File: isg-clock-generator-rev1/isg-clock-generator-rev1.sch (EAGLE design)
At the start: 162 parts, among them IC1 LMK03318RHSR, IC4 TPS7A8001DRBR, IC5 TPS7A8001DRBR, Q1 7M50072001, X1 OUT2_P, X2 OUT2_N, X3 OUT0_P, X4 PRIREF_P, X5 PRIREF_N, X6 V_IN_EXT

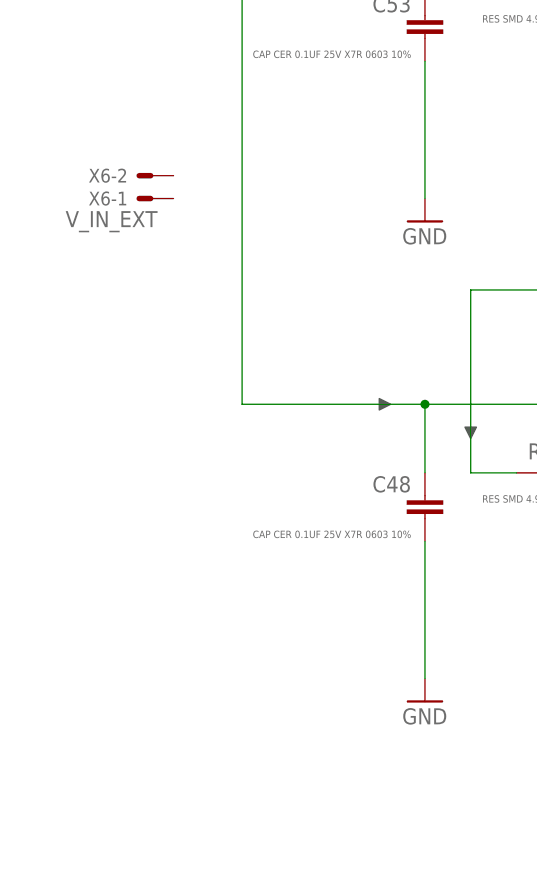
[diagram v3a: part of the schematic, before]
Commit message: First-pass routing done
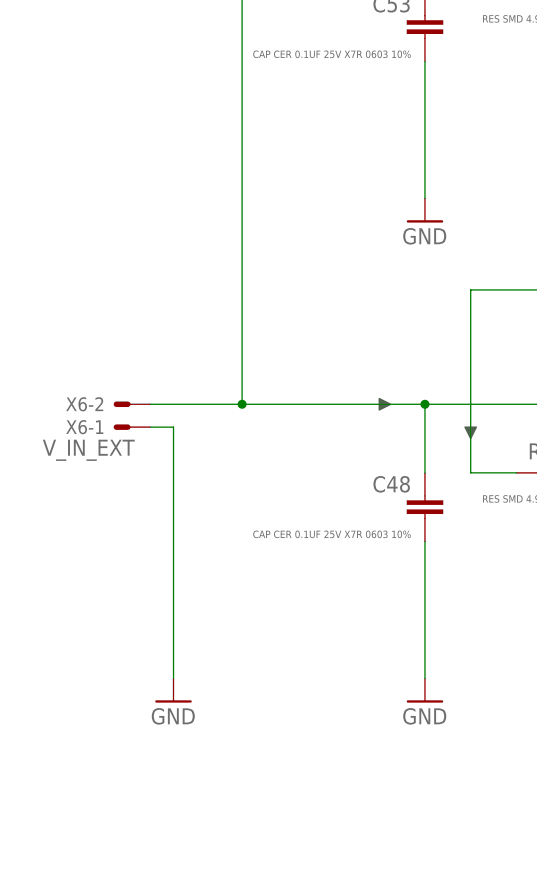
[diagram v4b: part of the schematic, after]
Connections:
- net GND: now also X6-1.S
- net VIN: now also X6-2.S
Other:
- note removed: "TODO: figure out power input connectors"
- moved on the sheet: X6-1, X6-2
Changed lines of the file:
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@@
 <part name="GND93" library="supply1" library_urn="urn:adsk.eagle:library:371" deviceset="GND" device=""/>
 <part name="R54" library="rcl-modified-footprints" deviceset="R-EU_" device="R0603" package3d_urn="urn:adsk.eagle:package:23555/2" value="0R JUMPER 0603"/>
+<part name="GND94" library="supply1" deviceset="GND" device=""/>
 </parts>
 <sheets>
@@
 <text x="124.46" y="416.56" size="1.778" layer="98">TODO: fix all values for new LDO MPN</text>
 <text x="312.42" y="416.56" size="3.81" layer="98">Headers for Connecting to Motherboard </text>
-<text x="15.24" y="416.56" size="1.778" layer="98">TODO: figure out power input connectors</text>
 <text x="86.36" y="335.28" size="1.27" layer="98">Vref(1+Rtop/Rbottom) = Vout</text>
 <text x="86.36" y="332.74" size="1.27" layer="98">Vref = 0.8V Nominal</text>
@@
 <attribute name="VALUE" x="347.98" y="409.575" size="1.778" layer="96"/>
 </instance>
-<instance part="X6" gate="-1" x="20.32" y="378.46" smashed="yes" rot="R180">
-<attribute name="NAME" x="17.78" y="379.222" size="1.524" layer="95" rot="R180"/>
-<attribute name="VALUE" x="21.082" y="377.063" size="1.778" layer="96" rot="R180"/>
-</instance>
-<instance part="X6" gate="-2" x="20.32" y="381" smashed="yes" rot="R180">
-<attribute name="NAME" x="17.78" y="381.762" size="1.524" layer="95" rot="R180"/>
+<instance part="X6" gate="-1" x="17.78" y="353.06" smashed="yes" rot="R180">
+<attribute name="NAME" x="15.24" y="353.822" size="1.524" layer="95" rot="R180"/>
+<attribute name="VALUE" x="18.542" y="351.663" size="1.778" layer="96" rot="R180"/>
+</instance>
+<instance part="X6" gate="-2" x="17.78" y="355.6" smashed="yes" rot="R180">
+<attribute name="NAME" x="15.24" y="356.362" size="1.524" layer="95" rot="R180"/>
 </instance>
 <instance part="C45" gate="G$1" x="167.64" y="396.24" smashed="yes">
@@
 <attribute name="NAME" x="276.86" y="112.268" size="1.778" layer="95"/>
 <attribute name="VALUE" x="277.368" y="110.49" size="0.8128" layer="96" rot="R270"/>
+</instance>
+<instance part="GND94" gate="1" x="22.86" y="322.58" smashed="yes">
+<attribute name="VALUE" x="20.32" y="320.04" size="1.778" layer="96"/>
 </instance>
 </instances>
@@
 <pinref part="C68" gate="G$1" pin="2"/>
 <wire x1="368.3" y1="50.8" x2="368.3" y2="53.34" width="0.1524" layer="91"/>
+</segment>
+<segment>
+<pinref part="GND94" gate="1" pin="GND"/>
+<wire x1="22.86" y1="325.12" x2="22.86" y2="353.06" width="0.1524" layer="91"/>
+<pinref part="X6" gate="-1" pin="S"/>
+<wire x1="22.86" y1="353.06" x2="20.32" y2="353.06" width="0.1524" layer="91"/>
 </segment>
 </net>
@@
 <wire x1="78.74" y1="353.06" x2="78.74" y2="355.6" width="0.1524" layer="91"/>
 <junction x="78.74" y="355.6"/>
-</segment>
-<segment>
+<pinref part="X6" gate="-2" pin="S"/>
+<wire x1="20.32" y1="355.6" x2="30.48" y2="355.6" width="0.1524" layer="91"/>
+<junction x="30.48" y="355.6"/>
+</segment>
+<segment>

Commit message: BOM and centroid files for assembly quote
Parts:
- removed C58, C62, C63: DNP, rcl-modified-footprints:C-EUC0603
- removed C59, C60: 0R JUMPER, rcl-modified-footprints:C-EUC0603
- removed C61: DNP 0603, rcl-modified-footprints:C-EUC0603
- removed C64: 0R JUMPER 0402, rcl-modified-footprints:C-EUC0402
- removed C65, C66, C67: CAP CER 0.1uF X7R 0402, rcl-modified-footprints:C-EUC0402
- removed C68: CAP CER 0.1UF 25V X7R 0603 10%, rcl-modified-footprints:C-EUC0603
- removed IC4, IC5: TPS7A8001DRBR, isg-clock-generator:TPS7A8001DRBR
- added C100, C101, C102, C103, C104, C105, C106, C107, C108, C109, C110, C111, C112: CAP CER 10uF 6.3V X5R 0603, rcl-modified-footprints:C-EUC0603
- added D1, D2: SL23HE3_A/I, diode:SCHOTTKY-DIODESMD
- added IC2, IC3: TPS7A8001DRBR, isg-clock-generator:TPS7A8001DRBR
- C1, C3: value CAP CER 10uF 6.3V X5R 0603 -> DNP
- C10: value CAP CER 0.01uF X7R 0402 -> DNP; device rcl-modified-footprints:C-EUC0402 -> rcl-modified-footprints:C-EUC0603
- C12, C20, C23, C24, C26, C30, C36, C4: value CAP CER 0.1uF X7R 0402 -> CAP CER 0.01uF X7R 0402
- C13, C34: value CAP CER 0.1uF X7R 0402 -> 0R JUMPER 0402
- C16, C17, C19, C25, C29, C33, C5: value CAP CER 10uF 6.3V X5R 0603 -> CAP CER 0.1uF X7R 0402; device rcl-modified-footprints:C-EUC0603 -> rcl-modified-footprints:C-EUC0402
- C18, C37: value CAP CER 10uF 6.3V X5R 0603 -> CAP CER 0.01uF X7R 0402; device rcl-modified-footprints:C-EUC0603 -> rcl-modified-footprints:C-EUC0402
- C2, C41: value CAP CER 10uF 6.3V X5R 0603 -> CAP CER 0.1UF 25V X7R 0603 10%
- C27, C31, C43, C8, C9: value CAP CER 0.01uF X7R 0402 -> CAP CER 0.1uF X7R 0402
- C35: value CAP CER 0.01uF X7R 0402 -> 0R JUMPER 0402
- C39: value CAP CER 0.01uF X7R 0402 -> CAP CER 0.1UF 25V X7R 0603 10%; device rcl-modified-footprints:C-EUC0402 -> rcl-modified-footprints:C-EUC0603
- C40, C42: value CAP CER 0.1uF X7R 0402 -> CAP CER 4.7UF 6.3V X5R 0603 10%; device rcl-modified-footprints:C-EUC0402 -> rcl-modified-footprints:C-EUC0603
- C44: value CAP CER 10000PF 25V X7R 0603 10% -> CAP CER 0.1uF X7R 0402; device rcl-modified-footprints:C-EUC0603 -> rcl-modified-footprints:C-EUC0402
- C45, C47: value CAP CER 4.7UF 6.3V X5R 0603 10% -> CAP CER 0.1uF X7R 0402; device rcl-modified-footprints:C-EUC0603 -> rcl-modified-footprints:C-EUC0402
- C46: value CAP CER 0.1UF 25V X7R 0603 10% -> 0R JUMPER 0603
- C48: value CAP CER 0.1UF 25V X7R 0603 10% -> DNP
- C50, C52: value 0R JUMPER 0402 -> CAP CER 0.1UF 25V X7R 0603 10%; device rcl-modified-footprints:C-EUC0402 -> rcl-modified-footprints:C-EUC0603
- C51: value CAP CER 0.1UF 25V X7R 0603 10% -> CAP CER 10000PF 25V X7R 0603 10%
- C53: value CAP CER 0.1UF 25V X7R 0603 10% -> CAP CER 3300pF X7R 0603
- C54: value CAP CER 0.01uF X7R 0402 -> CAP CER 0.033uF X7R 0603; device rcl-modified-footprints:C-EUC0402 -> rcl-modified-footprints:C-EUC0603
- C56: value CAP CER 0.033uF 0603 -> CAP CER 1UF 10V X7R 0603 10%
- C57: value CAP CER 3300pF 0603 -> CAP CER 1UF 10V X7R 0603 10%
- C7: value CAP CER 0.01uF X7R 0402 -> 0R JUMPER 0603; device rcl-modified-footprints:C-EUC0402 -> rcl-modified-footprints:C-EUC0603
- JP1: value EOS_MOTHERBOARD -> TI_USB2ANY; device isg-clock-generator:JP5Q -> Kramnik's Library:CON_OST_302-S101
- JP10: value REFSEL -> GPIO2
- JP11: value XO_MARGIN -> GPIO3; device isg-clock-generator:JP8Q -> isg-clock-generator:JP2E
- JP12: value LOOP_FILTER -> GPIO4; device isg-clock-generator:JP3Q -> isg-clock-generator:JP2E
- JP13: value PRIREF_VCM -> GPIO5
- JP14: value TI_USB2ANY -> XO_MARGIN; device Kramnik's Library:CON_OST_302-S101 -> isg-clock-generator:JP8Q
- JP3: value GPIO5 -> GPIO0
- JP4: value GPIO4 -> HWCTRL
- JP5: value GPIO3 -> REFSEL
- JP6: value GPIO2 -> EOS_MOTHERBOARD; device isg-clock-generator:JP2E -> isg-clock-generator:JP5Q
- JP7: value GPIO1 -> PRIREF_VCM
- JP8: value GPIO0 -> LOOP_FILTER; device isg-clock-generator:JP2E -> isg-clock-generator:JP3Q
- JP9: value HWCTRL -> GPIO1
- LED1: value STAT0=LO -> STAT1=LO
- LED2: value STAT1=LO -> STAT0=LO
- R1, R2: value RES SMD 510R 0603 -> RES SMD 510 OHM 1% 1/10W 0603
- R10, R14, R18: value RES SMD 4.99K OHM 1% 1/10W 0603 -> DNP
- R11, R8, R9: device rcl-modified-footprints:R-EU_R0402 -> rcl-modified-footprints:R-EU_R0603
- R12, R13: value DNP -> RES SMD 10K OHM 1% 1/10W 0603; device rcl-modified-footprints:R-EU_R0402 -> rcl-modified-footprints:R-EU_R0603
- R15: value RES SMD 1.62K OHM 1% 1/10W 0603 -> DNP; device rcl-modified-footprints:R-EU_R0603 -> rcl-modified-footprints:R-EU_R0402
- R16: value RES SMD 1K OHM 1% 1/10W 0603 -> DNP; device rcl-modified-footprints:R-EU_R0603 -> rcl-modified-footprints:R-EU_R0402
- R17: value RES SMD 4.99K OHM 1% 1/10W 0603 -> 0R JUMPER 0402; device rcl-modified-footprints:R-EU_R0603 -> rcl-modified-footprints:R-EU_R0402
- R19: value RES SMD 0 OHM 1% 1/10W 0603 -> DNP
- R20: value RES SMD 2.32K OHM 1% 1/10W 0603 -> 0R JUMPER 0402; device rcl-modified-footprints:R-EU_R0603 -> rcl-modified-footprints:R-EU_R0402
- R21: value RES SMD 5.62K OHM 1% 1/10W 0603 -> 0R JUMPER 0402; device rcl-modified-footprints:R-EU_R0603 -> rcl-modified-footprints:R-EU_R0402
- R22: value RES SMD 10.5K OHM 1% 1/10W 0603 -> DNP; device rcl-modified-footprints:R-EU_R0603 -> rcl-modified-footprints:R-EU_R0402
- R23: value RES SMD 18.7K OHM 1% 1/10W 0603 -> DNP; device rcl-modified-footprints:R-EU_R0603 -> rcl-modified-footprints:R-EU_R0402
- R24: value RES SMD 34.8K OHM 1% 1/10W 0603 -> DNP; device rcl-modified-footprints:R-EU_R0603 -> rcl-modified-footprints:R-EU_R0402
- R25: value RES SMD 84.5K OHM 1% 1/10W 0603 -> DNP; device rcl-modified-footprints:R-EU_R0603 -> rcl-modified-footprints:R-EU_R0402
- R26: value DNP -> RES SMD 3.92K OHM 1% 1/10W 0603
- R27, R33: value RES SMD 1K OHM 1% 1/10W 0603 -> RES SMD 4.99K OHM 1% 1/10W 0603
- R28: value DNP -> RES SMD 1.62K OHM 1% 1/10W 0603
- R29: value DNP -> RES SMD 4.99K OHM 1% 1/10W 0603
- R3: value 0R JUMPER 0402 -> DNP; device rcl-modified-footprints:R-EU_R0402 -> rcl-modified-footprints:R-EU_R0603
- R30: value RES SMD 1K OHM 1% 1/10W 0603 -> 0R JUMPER 0603
- R31, R34: value RES SMD 13.0K OHM 1% 1/10W 0603 -> RES SMD 4.99K OHM 1% 1/10W 0603
- R36: value RES SMD 1K OHM 1% 1/10W 0603 -> DNP
- R37, R39: value RES SMD 13.0K OHM 1% 1/10W 0603 -> RES SMD 1K OHM 1% 1/10W 0603
- R38: value RES SMD 4.99K OHM 1% 1/10W 0603 -> RES SMD 1K OHM 1% 1/10W 0603
- R4: value 0R JUMPER 0402 -> RES SMD 10K OHM 1% 1/10W 0603; device rcl-modified-footprints:R-EU_R0402 -> rcl-modified-footprints:R-EU_R0603
- R40: value RES SMD 10K OHM 1% 1/10W 0603 -> RES SMD 1K OHM 1% 1/10W 0603
- R41: value DNP -> RES SMD 1K OHM 1% 1/10W 0603
- R42: value DNP -> 0R JUMPER 0603
- R43: value RES SMD 1K OHM 1% 1/10W 0603 -> RES SMD 13.0K OHM 1% 1/10W 0603
- R44, R45: value DNP -> RES SMD 13.0K OHM 1% 1/10W 0603
- R46, R54: value 0R JUMPER 0603 -> DNP
- R47: value RES SMD 1K OHM 1% 1/10W 0603 -> RES SMD 0 OHM 1% 1/10W 0603
- R48: value RES SMD 1K OHM 1% 1/10W 0603 -> RES SMD 2.32K OHM 1% 1/10W 0603
- R49: value DNP -> RES SMD 5.62K OHM 1% 1/10W 0603
- R5: value 0R JUMPER 0402 -> RES SMD 1K OHM 1% 1/10W 0603; device rcl-modified-footprints:R-EU_R0402 -> rcl-modified-footprints:R-EU_R0603
- R50: value DNP -> RES SMD 10.5K OHM 1% 1/10W 0603
- R51: value DNP 0603 -> RES SMD 18.7K OHM 1% 1/10W 0603
- R52: value DNP 0603 -> RES SMD 34.8K OHM 1% 1/10W 0603
- R53: value DNP -> RES SMD 84.5K OHM 1% 1/10W 0603
- R6: value DNP -> RES SMD 13.0K OHM 1% 1/10W 0603; device rcl-modified-footprints:R-EU_R0402 -> rcl-modified-footprints:R-EU_R0603
- R7: value RES SMD 3.92K OHM 1% 1/10W 0603 -> DNP
- X1: value OUT2_P -> OUT0_P
- X2: value OUT2_N -> PRIREF_N
- X3: value OUT0_P -> OUT2_P
- X5: value PRIREF_N -> OUT2_N
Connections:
- removed net GPIO0: IC1.GPIO0, R39.2
- removed net N$10: JP14.3
- removed net N$11: JP14.1
- removed net N$12: JP14.8
- removed net N$13: JP14.4
- removed net N$14: JP14.2
- removed net N$9: JP14.7
- new net GPIO0/SYNC: IC1.GPIO0, JP1.1, R6.2
- new net NC_USB2ANY_CONN_1: JP1.7
- new net NC_USB2ANY_CONN_2: JP1.8
- new net VIN_EXT: D2.A, X6-2.S
- new net VIN_MLB: D1.A, JP6.1, JP6.2
- net DECAP_DIG: now also C102.1; no longer C1.1
- net DECAP_LDO: now also C110.1; no longer C3.1
- net DECAP_PLL: now also C111.1; no longer C2.1
- net EXT_VDD: now also JP1.5, R3.1; no longer JP14.5, R53.1
- net GND: now also C100.2, C101.2, C102.2, C103.2, C104.2, C105.2, C106.2, C107.2, C108.2, C109.2, C110.2, C111.2, C112.2, C50.2, C52.2, IC2.GND, IC3.GND, JP12.1, JP14.1, JP14.11, JP14.13, JP14.15, JP14.3, JP14.5, JP14.7, JP14.9, JP6.3, JP6.4, JP6.6, R10.1, R16.1, R19.1, R22.1, R24.1, R26.2, R28.2, R33.1, R34.1, R36.1, R9.1; no longer C13.2, C34.2, C35.2, C46.2, C58.2, C61.2, C62.2, C63.2, C65.2, C66.2, C67.2, C68.2, C7.2, IC4.GND, IC5.GND, JP1.3, JP1.4, JP11.11, JP11.13, JP11.15, JP11.3, JP11.5, JP11.7, JP11.9, JP14.6, JP6.1, JP8.1, R11.1, R12.1, R13.1, R15.2, R29.1, R32.1, R38.1, R42.1, R45.1, R52.1, R7.2
- net GPIO0_JUMPER: now also JP3.2, R6.1; no longer JP8.2, R39.1
- net GPIO1: now also R33.2, R37.2, R43.1; no longer R36.2, R37.1, R38.2
- net GPIO1_JUMPER: now also JP9.2, R37.1; no longer JP7.2, R36.1
- net GPIO2: now also R34.2, R38.2, R44.1; no longer R33.2, R34.1, R35.2
- net GPIO2_JUMPER: now also JP10.2, R38.1; no longer JP6.2, R33.1
- net GPIO3: now also R35.2, R39.2, R45.1; no longer R30.2, R31.1, R32.2
- net GPIO3_JUMPER: now also JP11.2, R39.1; no longer JP5.2, R30.1
- net GPIO4: now also R36.2, R40.2, R46.1; no longer R27.2, R28.1, R29.2
- net GPIO4_JUMPER: now also JP12.2, R40.1; no longer JP4.2, R27.1
- net GPIO5: now also R42.1; no longer R54.1
- net GPIO5_JUMPER: now also JP13.2, R42.2, R47.1, R48.1, R49.1, R50.1, R51.1, R52.1, R53.1, R54.1; no longer JP3.2, R19.1, R20.1, R21.1, R22.1, R23.1, R24.1, R25.1, R26.1, R54.2
- net GPIO5_SEL_11_12: now also JP14.12, R52.2; no longer JP11.12, R24.2
- net GPIO5_SEL_13_14: now also JP14.14, R53.2; no longer JP11.14, R25.2
- net GPIO5_SEL_15_16: now also JP14.16, R54.2; no longer JP11.16, R26.2
- net GPIO5_SEL_1_2: now also JP14.2, R47.2; no longer JP11.2, R19.2
- net GPIO5_SEL_3_4: now also JP14.4, R48.2; no longer JP11.4, R20.2
- net GPIO5_SEL_5_6: now also JP14.6, R49.2; no longer JP11.6, R21.2
- net GPIO5_SEL_7_8: now also JP14.8, R50.2; no longer JP11.8, R22.2
- net GPIO5_SEL_9_10: now also JP14.10, R51.2; no longer JP11.10, R23.2
- net HWCTRL_JUMPER: now also JP4.2, R4.1; no longer JP9.2, R40.1
- net HW_SW_CTRL: now also JP1.3, JP6.8, R4.2, R7.1, R9.2; no longer JP1.8, R40.2, R41.1, R42.2
- net LDO_PVCORE_EN: now also IC3.EN, R32.2; no longer IC4.EN, R18.2
- net LDO_PVCORE_FB: now also IC3.FB/SNS, R28.1, R29.1; no longer IC4.FB/SNS, R14.1, R15.1
- net LDO_PVCORE_SS: now also C51.1, IC3.NR/SS; no longer C49.1, IC4.NR/SS
- net LDO_PVDDIO_EN: now also IC2.EN, R31.2; no longer IC5.EN, R17.2
- net LDO_PVDDIO_FB: now also IC2.FB/SNS, R26.1, R27.1; no longer IC5.FB/SNS, R10.1, R7.1
- net LDO_PVDDIO_SS: now also C49.1, IC2.NR/SS; no longer C44.1, IC5.NR/SS
- net LF1: now also C48.1, R30.1; no longer C58.1, R46.1
- net LF_FRAC_N: now also C54.1, JP8.3; no longer C56.1, JP12.3
- net LF_INT_N\: now also C53.1, JP8.1; no longer C57.1, JP12.1
- net LF_NARROW: now also JP8.5; no longer JP12.5
- net LF_R: now also JP8.2, JP8.4, JP8.6, R30.2; no longer JP12.2, JP12.4, JP12.6, R46.2
- net OUT0_P: now also R17.2; no longer R5.2
- net OUT0_R_C_P: now also C13.2, R15.1, R16.2, X1.1; no longer C64.2, R13.2, R9.1, X3.1
- net OUT0_R_P: now also C13.1, R17.1; no longer C64.1, R5.1
- net OUT2_N: now also R21.2; no longer R4.2
- net OUT2_P: now also R20.2; no longer R3.2
- net OUT2_R_C_N: now also C35.2, R24.2, R25.1, X5.1; no longer C52.2, R12.2, R8.1, X2.1
- net OUT2_R_C_P: now also C34.2, R22.2, R23.1, X3.1; no longer C50.2, R11.2, R6.1, X1.1
- net OUT2_R_N: now also C35.1, R21.1; no longer C52.1, R4.1
- net OUT2_R_P: now also C34.1, R20.1; no longer C50.1, R3.1
- net PDN: now also C4.1, JP1.2; no longer C54.1
- net PP_P1V8_VDDO: now also C14.1, C15.1, C19.1, C22.1, C25.1, C29.1, C32.1, C33.1, C39.1, C40.1, C45.1, IC2.OUT, IC2.OUT_2, L3.P$2, L4.P$2, L5.P$2, R15.2, R23.2, R25.2, R27.2; no longer C26.1, C30.1, C34.1, C38.1, C42.1, C46.1, C47.1, C6.1, C65.1, C66.1, C67.1, IC5.OUT, IC5.OUT_2, L1.P$2, L10.P$2, L9.P$2, R10.2, R6.2, R8.2, R9.2
- net PP_P3V3_PLL_CORE: now also C2.1, C41.1, C42.1, C43.1, C47.1, C5.1, C6.1, IC3.OUT, IC3.OUT_2, JP11.3, JP12.3, JP3.3, L1.P$1, L10.P$1, L9.P$1, R12.2, R13.2, R18.2, R29.2, R3.2, R31.1, R43.2, R45.2, R46.2, R7.2, R8.2; no longer C20.1, C21.1, C22.1, C23.1, C45.1, C51.1, C68.1, IC4.OUT, IC4.OUT_2, JP6.3, JP7.3, JP8.3, L3.P$1, L4.P$1, L5.P$1, R14.2, R16.2, R17.1, R28.2, R31.2, R34.2, R37.2, R47.2, R48.2, R51.2, R53.2
- net PRIREF_N: now also C7.2, R11.2; no longer C60.2, R50.2
- net PRIREF_P: now also C46.2, R14.2; no longer C59.2, R49.2
- net PRIREF_R_N: now also C7.1, X2.1; no longer C60.1, X5.1
- net PRIREF_R_P: now also C46.1; no longer C59.1
- net PRIREF_VCM: now also C1.1, JP7.2, R11.1, R14.1; no longer C61.1, JP13.2, R49.1, R50.1
- net PRIREF_VCM_DIVIDER: now also JP7.3, R18.1, R19.2; no longer JP13.3, R51.1, R52.2
- net PULLUP_GPIO5: now also JP13.3, R41.1; no longer JP3.3, R16.1
- net REFSEL: now also JP1.4, R10.2, R5.2, R8.1; no longer R43.2, R44.1, R45.2
- net REFSEL_JUMPER: now also JP5.2, R5.1; no longer JP10.2, R43.1
- net SCL: now also JP1.9, JP6.10, R13.1; no longer JP1.10, JP14.9, R47.1
- net SDA: now also JP1.10, JP6.9, R12.1; no longer JP1.9, JP14.10, R48.1
- net SECREF_N: now also C10.1; no longer C62.1
- net SECREF_P: now also C3.1; no longer C63.1
- net STATUS0: now also JP6.7, LED2.C; no longer JP1.7, LED1.C
- net STATUS1: now also JP6.5, LED1.C; no longer JP1.5, LED2.C
- net VDDO_01: now also C104.1, C16.1, C20.1, L4.P$1; no longer C4.1, C5.1, C7.1, L1.P$1
- net VDDO_23: now also C106.1, C24.1, C27.1, L6.P$1; no longer C40.1, C41.1, C43.1, L10.P$1
- net VDDO_4: now also C108.1, C30.1, C31.1, L8.P$1; no longer C36.1, C37.1, C39.1, L9.P$1
- net VDDO_5: now also C107.1, C26.1, C28.1, L7.P$1; no longer C32.1, C33.1, C35.1, L8.P$1
- net VDDO_6: now also C105.1, C21.1, C23.1, L5.P$1; no longer C28.1, C29.1, C31.1, L7.P$1
- net VDDO_7: now also C103.1, C17.1, C18.1, L3.P$1; no longer C24.1, C25.1, C27.1, L6.P$1
- net VDD_DIG: now also C101.1, C12.1, C9.1; no longer C11.1, C15.1, C16.1
- net VDD_IN: now also C100.1, C11.1, C8.1, L1.P$2; no longer C10.1, C14.1, C17.1, L3.P$2
- net VDD_LDO: now also C109.1, C36.1, C44.1, L10.P$2; no longer C12.1, C19.1, C8.1, L5.P$2
- net VDD_PLL: now also C112.1, C37.1, C38.1, L9.P$2; no longer C13.1, C18.1, C9.1, L4.P$2
- net VIN: now also C50.1, C52.1, C56.1, C57.1, D1.C, D2.C, IC2.IN, IC2.IN_2, IC3.IN, IC3.IN_2, R32.1; no longer C48.1, C53.1, IC4.IN, IC4.IN_2, IC5.IN, IC5.IN_2, JP1.1, JP1.2, R18.1, X6-2.S
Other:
- note added: "("U2A_GPIO4")"
- note added: "("U2A_GPIO5")"
- note added: "("U2A_GPIO6")"
- note added: "("U2A_GPIO7")"
- note added: "30V, 2A Rating 395mV drop @ 1A Si Schottky"
- note added: "MAX VIN IS ONLY 7V!"
- note added: "SMB Package OR Diodes"
- note added: "TI USB2ANY connector Note: The pins are numbered differently than on the eval board Double check this against the cable pinout"
- note removed: "TI USB2ANY connector"
- moved on the sheet: C1, C10, C11, C12, C13, C14, C15, C16, C17, C18, C19, C2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
